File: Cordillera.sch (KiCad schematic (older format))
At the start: 29 parts, among them Q1 AO3400, Q2 AO3400, SW1 SW_SPST, U1 STM32F072CBTx, U2 XC6206P332MR, U3 SRV05-4

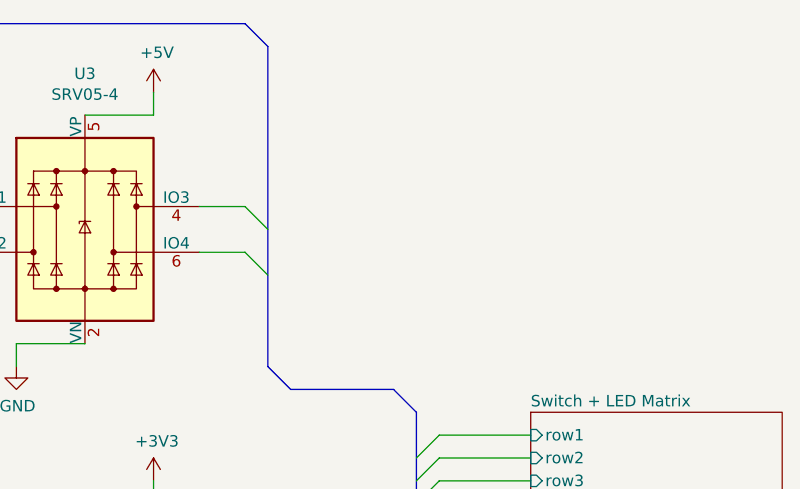
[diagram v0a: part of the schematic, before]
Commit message: Add indicator LEDs
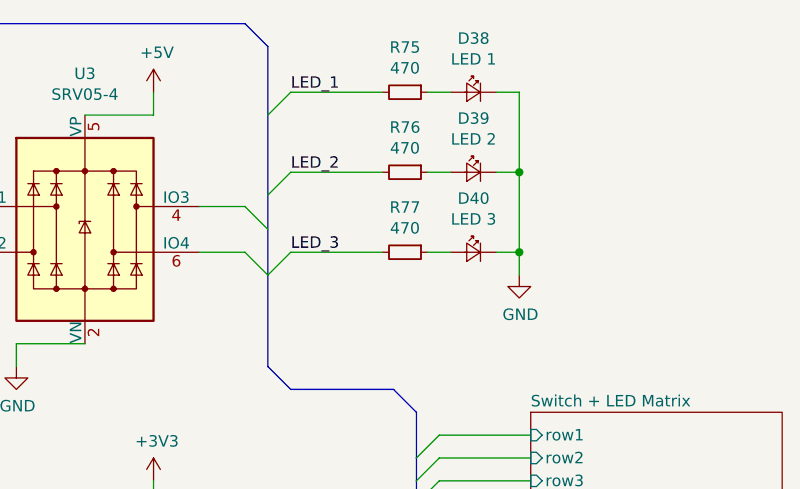
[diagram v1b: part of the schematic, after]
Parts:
- added D38: LED 1, keeb_lighting:LED_D3.0mm, symbol keeb_lighting:LED_Small
- added D39: LED 2, keeb_lighting:LED_D3.0mm, symbol keeb_lighting:LED_Small
- added D40: LED 3, keeb_lighting:LED_D3.0mm, symbol keeb_lighting:LED_Small
- added R75, R76, R77: 470, keeb_parts:R_0603_1608Metric, symbol keeb_parts:R_Small
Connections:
- net GND: now also D38.1 (K), D39.1 (K), D40.1 (K)
- new net: D38.2 (A), R75.1
- new net: D39.2 (A), R76.1
- new net: D40.2 (A), R77.1
- new net LED_1: R75.2
- new net LED_2: R76.2
- new net LED_3: R77.2
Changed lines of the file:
@@
+	1    0    0    -1
+$EndComp
+$Comp
+L keeb_lighting:LED_Small D38
+U 1 1 5F8AAE9D
+P 7450 1150
+F 0 "D38" H 7450 1385 50  0000 C CNN
+F 1 "LED 1" H 7450 1294 50  0000 C CNN
+F 2 "keeb_lighting:LED_D3.0mm" V 7450 1150 50  0001 C CNN
+F 3 "~" V 7450 1150 50  0001 C CNN
+	1    7450 1150
+	-1   0    0    -1
+$EndComp
+$Comp
+L keeb_lighting:LED_Small D39
+U 1 1 5F8AC84D
+P 7450 1500
+F 0 "D39" H 7450 1735 50  0000 C CNN
+F 1 "LED 2" H 7450 1644 50  0000 C CNN
+F 2 "keeb_lighting:LED_D3.0mm" V 7450 1500 50  0001 C CNN
+F 3 "~" V 7450 1500 50  0001 C CNN
+	1    7450 1500
+	-1   0    0    -1
+$EndComp
+$Comp
+L keeb_lighting:LED_Small D40
+U 1 1 5F8ACDD5
+P 7450 1850
+F 0 "D40" H 7450 2085 50  0000 C CNN
+F 1 "LED 3" H 7450 1994 50  0000 C CNN
+F 2 "keeb_lighting:LED_D3.0mm" V 7450 1850 50  0001 C CNN
+F 3 "~" V 7450 1850 50  0001 C CNN
+	1    7450 1850
+	-1   0    0    -1
+$EndComp
+$Comp
+L keeb_parts:R_Small R75
+U 1 1 5F8B84D2
+P 7150 1150
+F 0 "R75" V 6954 1150 50  0000 C CNN
+F 1 "470" V 7045 1150 50  0000 C CNN
+F 2 "keeb_parts:R_0603_1608Metric" H 7150 1150 50  0001 C CNN
+F 3 "~" H 7150 1150 50  0001 C CNN
+	1    7150 1150
+	0    1    1    0
+$EndComp
+Wire Wire Line
+	7350 1150 7250 1150
+$Comp
+L keeb_parts:R_Small R76
+U 1 1 5F8C72A6
+P 7150 1500
+F 0 "R76" V 6954 1500 50  0000 C CNN
+F 1 "470" V 7045 1500 50  0000 C CNN
+F 2 "keeb_parts:R_0603_1608Metric" H 7150 1500 50  0001 C CNN
+F 3 "~" H 7150 1500 50  0001 C CNN
+	1    7150 1500
+	0    1    1    0
+$EndComp
+Wire Wire Line
+	7350 1500 7250 1500
+$Comp
+L keeb_parts:R_Small R77
+U 1 1 5F8D1CE0
+P 7150 1850
+F 0 "R77" V 6954 1850 50  0000 C CNN
+F 1 "470" V 7045 1850 50  0000 C CNN
+F 2 "keeb_parts:R_0603_1608Metric" H 7150 1850 50  0001 C CNN
+F 3 "~" H 7150 1850 50  0001 C CNN
+	1    7150 1850
+	0    1    1    0
+$EndComp
+Wire Wire Line
+	7350 1850 7250 1850
+Wire Wire Line
+	7050 1500 6650 1500
+Entry Wire Line
+	6650 1500 6550 1600
+Text Label 6650 1500 0    50   ~ 0
+LED_2
+Wire Wire Line
+	7050 1850 6650 1850
+Entry Wire Line
+	6650 1850 6550 1950
+Text Label 6650 1850 0    50   ~ 0
+LED_3
+Wire Wire Line
+	7050 1150 6650 1150
+Entry Wire Line
+	6650 1150 6550 1250
+Text Label 6650 1150 0    50   ~ 0
+LED_1
+Wire Wire Line
+	7550 1150 7650 1150
+Wire Wire Line
+	7650 1150 7650 1500
+Wire Wire Line
+	7650 1850 7550 1850
+Wire Wire Line
+	7550 1500 7650 1500
+Connection ~ 7650 1500
+Wire Wire Line
+	7650 1500 7650 1850
+Wire Wire Line
+	7650 1850 7650 1950
+Connection ~ 7650 1850
+$Comp
+L keeb_power:GND #PWR0102
+U 1 1 5F93905E
+P 7650 1950
+F 0 "#PWR0102" H 7650 1700 50  0001 C CNN
+F 1 "GND" H 7655 1777 50  0000 C CNN
+F 2 "" H 7650 1950 50  0001 C CNN
+F 3 "" H 7650 1950 50  0001 C CNN
+	1    7650 1950
 	1    0    0    -1
 $EndComp

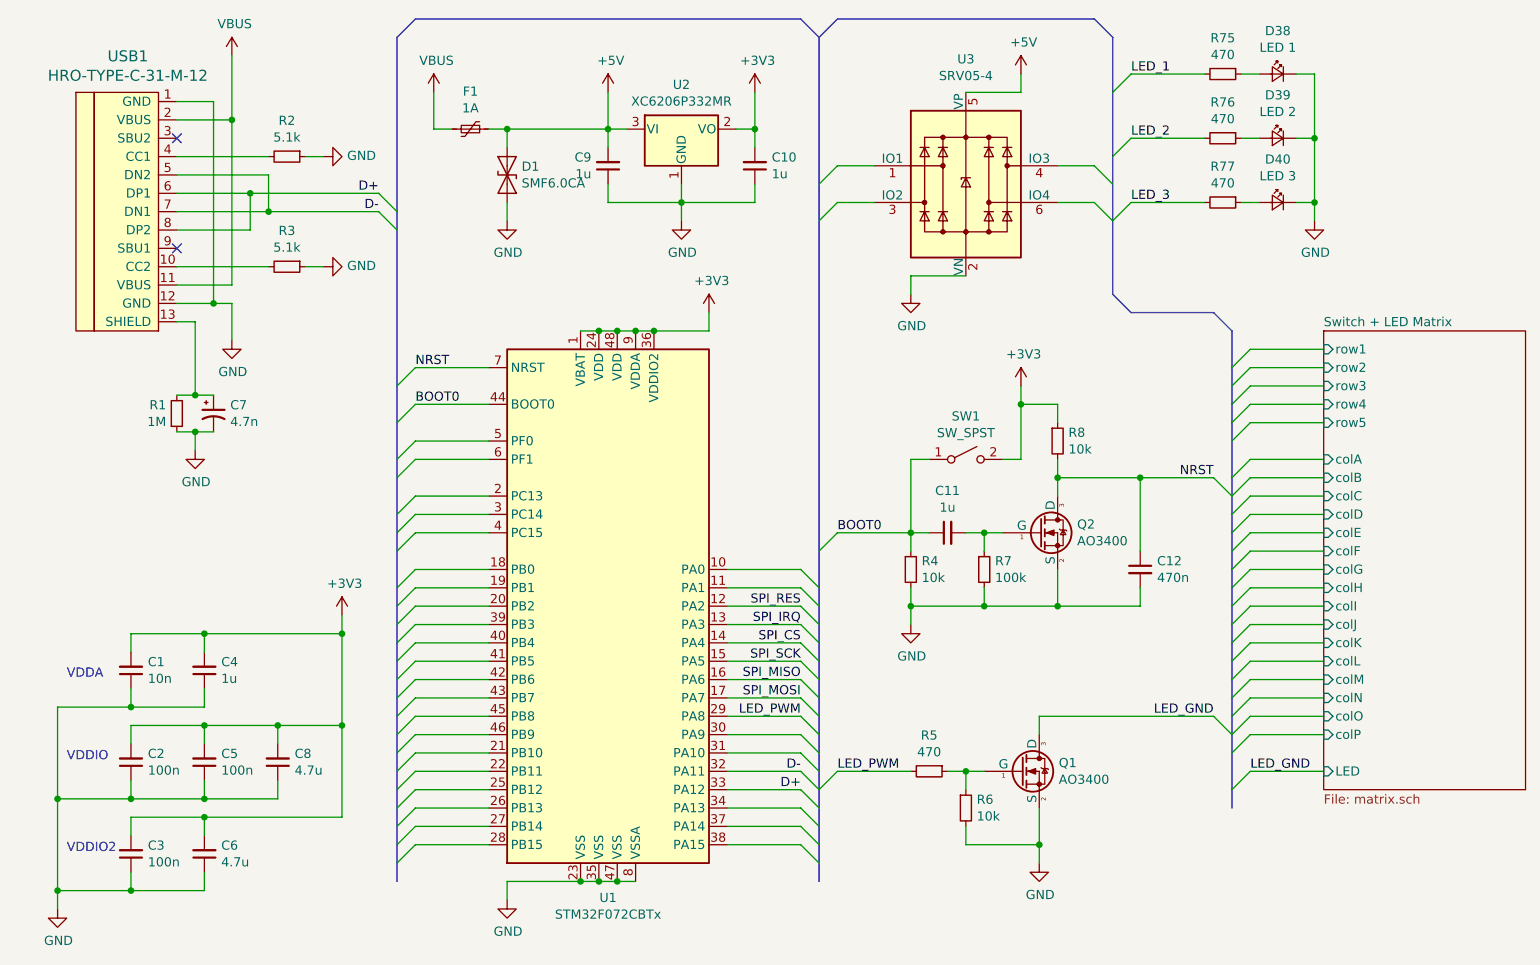
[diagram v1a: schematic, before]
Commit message: Finish routing switches
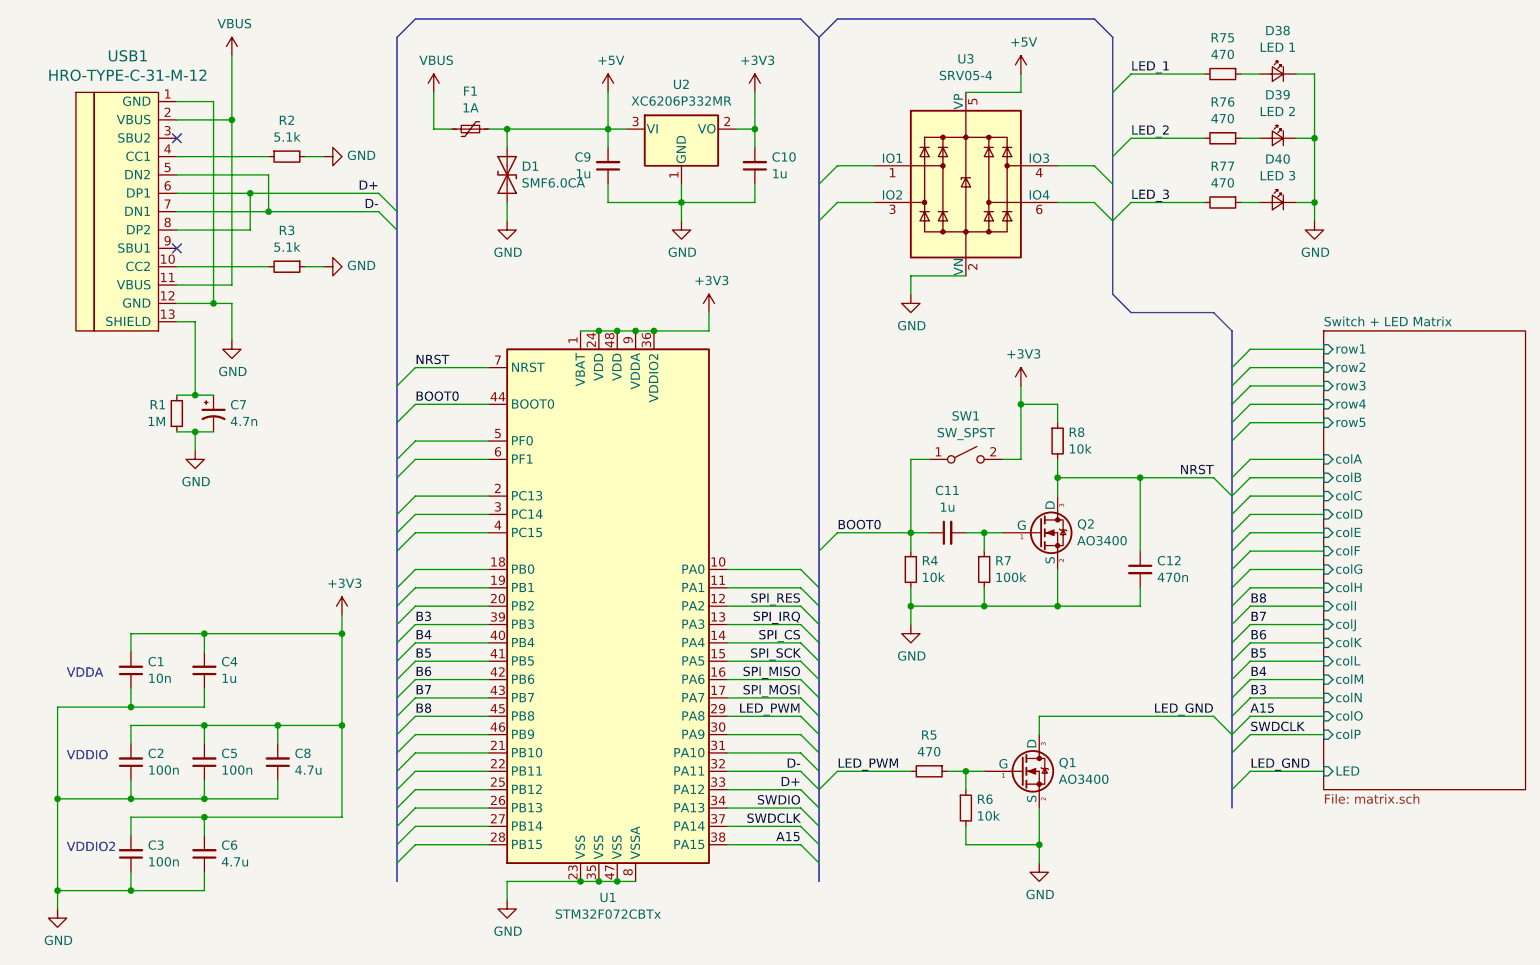
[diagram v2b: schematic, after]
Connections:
- net GND: now also R2.2; no longer R2.1
- net at USB1.4 (CC1): now also R2.1; no longer R2.2
- net SWDIO: now reaches U1.34 (PA13)
- net SWDCLK: now reaches U1.37 (PA14)
- net A15: now reaches U1.38 (PA15)
- net B3: now reaches U1.39 (PB3)
- net B4: now reaches U1.40 (PB4)
- net B5: now reaches U1.41 (PB5)
- net B6: now reaches U1.42 (PB6)
- net B7: now reaches U1.43 (PB7)
- net B8: now reaches U1.45 (PB8)
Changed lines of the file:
@@
 	1450 1600 1950 1600
-$Comp
-L keeb_parts:R_Small R2
-U 1 1 5F3187E0
-P 2050 1600
-F 0 "R2" V 1854 1600 50  0000 C CNN
-F 1 "5.1k" V 1945 1600 50  0000 C CNN
-F 2 "keeb_parts:R_0603_1608Metric" H 2050 1600 50  0001 C CNN
-F 3 "~" H 2050 1600 50  0001 C CNN
-	1    2050 1600
-	0    1    1    0
-$EndComp
 $Comp
 L keeb_parts:R_Small R3
@@
 	1    0    0    -1
 $EndComp
+Text Label 2750 4550 0    50   ~ 0
+B7
+Text Label 2750 4450 0    50   ~ 0
+B6
+Text Label 2750 4350 0    50   ~ 0
+B5
+Text Label 2750 4250 0    50   ~ 0
+B4
+Text Label 2750 4150 0    50   ~ 0
+B3
+Text Label 4850 5350 2    50   ~ 0
+A15
+Text Label 4850 5250 2    50   ~ 0
+SWDCLK
+Text Label 4850 5150 2    50   ~ 0
+SWDIO
+Text Label 2750 4650 0    50   ~ 0
+B8
+Text Label 7300 4750 0    50   ~ 0
+SWDCLK
+Text Label 7300 4650 0    50   ~ 0
+A15
+Text Label 7300 4550 0    50   ~ 0
+B3
+Text Label 7300 4450 0    50   ~ 0
+B4
+Text Label 7300 4350 0    50   ~ 0
+B5
+Text Label 7300 4250 0    50   ~ 0
+B6
+Text Label 7300 4150 0    50   ~ 0
+B7
+Text Label 7300 4050 0    50   ~ 0
+B8
+Wire Bus Line
+	7200 2550 7200 5150
 Wire Bus Line
 	6550 950  6550 2350
-Wire Bus Line
-	7200 2550 7200 5150
 Wire Bus Line
 	4950 950  4950 5550
 Wire Bus Line
 	2650 950  2650 5550
+$Comp
+L keeb_parts:R_Small R2
+U 1 1 5F3187E0
+P 2050 1600
+F 0 "R2" V 1854 1600 50  0000 C CNN
+F 1 "5.1k" V 1945 1600 50  0000 C CNN
+F 2 "keeb_parts:R_0603_1608Metric" H 2050 1600 50  0001 C CNN
+F 3 "~" H 2050 1600 50  0001 C CNN
+	1    2050 1600
+	0    -1   1    0
+$EndComp
 $EndSCHEMATC

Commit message: Finish column routing
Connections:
- net B2: now reaches U1.20 (PB2)
- net B10: now reaches U1.21 (PB10)
- net B11: now reaches U1.22 (PB11)
- net B12: now reaches U1.25 (PB12)
- net B13: now reaches U1.26 (PB13)
- net B14: now reaches U1.27 (PB14)
- net B15: now reaches U1.28 (PB15)
- net A9: now reaches U1.30 (PA9)
- net B9: now reaches U1.46 (PB9)
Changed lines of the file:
@@
 	7700 3050 7300 3050
-Wire Wire Line
-	7700 3250 7300 3250
-Wire Wire Line
-	7700 3350 7300 3350
-Wire Wire Line
-	7700 3450 7300 3450
-Wire Wire Line
-	7700 3550 7300 3550
-Wire Wire Line
-	7700 3650 7300 3650
-Wire Wire Line
-	7700 3750 7300 3750
 Wire Wire Line
 	7700 3850 7300 3850
@@
 Text Label 7300 4050 0    50   ~ 0
 B8
-Wire Bus Line
-	7200 2550 7200 5150
-Wire Bus Line
-	6550 950  6550 2350
-Wire Bus Line
-	4950 950  4950 5550
-Wire Bus Line
-	2650 950  2650 5550
 $Comp
 L keeb_parts:R_Small R2
@@
 	0    -1   1    0
 $EndComp
+Text Label 2750 4750 0    50   ~ 0
+B9
+Text Label 7300 2750 0    50   ~ 0
+B9
+Text Label 7300 2650 0    50   ~ 0
+SWDIO
+Text Label 4850 4750 2    50   ~ 0
+A9
+Text Label 7300 3950 0    50   ~ 0
+A9
+Text Label 2750 5050 0    50   ~ 0
+B12
+Text Label 2750 5150 0    50   ~ 0
+B13
+Text Label 2750 5250 0    50   ~ 0
+B14
+Text Label 2750 5350 0    50   ~ 0
+B15
+Wire Wire Line
+	7700 3550 7300 3550
+Wire Wire Line
+	7700 3450 7300 3450
+Wire Wire Line
+	7700 3350 7300 3350
+Wire Wire Line
+	7700 3250 7300 3250
+Text Label 7300 3550 0    50   ~ 0
+B12
+Text Label 7300 3450 0    50   ~ 0
+B13
+Text Label 7300 3350 0    50   ~ 0
+B14
+Text Label 7300 3250 0    50   ~ 0
+B15
+Text Label 2750 4950 0    50   ~ 0
+B11
+Text Label 2750 4850 0    50   ~ 0
+B10
+Wire Wire Line
+	7700 3750 7300 3750
+Wire Wire Line
+	7700 3650 7300 3650
+Text Label 7300 3650 0    50   ~ 0
+B11
+Text Label 7300 3750 0    50   ~ 0
+B10
+Wire Bus Line
+	6550 950  6550 2350
+Wire Bus Line
+	7200 2550 7200 5150
+Wire Bus Line
+	4950 950  4950 5550
+Wire Bus Line
+	2650 950  2650 5550
+Text Label 2750 4050 0    50   ~ 0
+B2
+Text Label 7300 3850 0    50   ~ 0
+B2
 $EndSCHEMATC

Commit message: Update files
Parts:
- added H1, H2: MountingHole, keeb_misc:mounting-circular, symbol keeb_parts:MountingHole
- added J1: Conn_01x08, keeb_connectors:PinHeader_2x04_P2.54mm_Vertical, symbol keeb_connectors:Conn_01x08
- C1, C10, C2, C3, C4, C5, C6, C7, C8, C9: footprint keeb_parts:R_0603_1608Metric -> keeb_parts:C_0603_1608Metric
- C11: value 1u -> 4.7u; footprint keeb_parts:R_0603_1608Metric -> keeb_parts:C_0603_1608Metric
- C12: value 470n -> 1u; footprint keeb_parts:R_0603_1608Metric -> keeb_parts:C_0603_1608Metric
- Q1, Q2: value AO3400 -> 2N7002
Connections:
- net LED_1 is gone; now on net B0: R75.2
- net LED_2 is gone; now on net A1: R76.2
- net LED_3 is gone; now on net A0: R77.2
- net +3V3: now also R8.2, J1.8 (Pin_8); no longer R8.1
- net D+: now also U3.1 (IO1), U3.3 (IO2)
- net D-: now also U3.4 (IO3), U3.6 (IO4)
- net GND: now also J1.7 (Pin_7)
- net NRST: now also R8.1; no longer R8.2
- net SPI_CS: now also J1.4 (Pin_4)
- net SPI_IRQ: now also J1.5 (Pin_5)
- net SPI_MISO: now also J1.2 (Pin_2)
- net SPI_MOSI: now also J1.3 (Pin_3)
- net SPI_RES: now also J1.6 (Pin_6)
- net SPI_SCK: now also J1.1 (Pin_1)
- net A0: now reaches U1.10 (PA0)
- net A1: now reaches U1.11 (PA1)
- net B0: now reaches U1.18 (PB0)
- net B1: now reaches U1.19 (PB1)
- net C13: now reaches U1.2 (PC13)
- net C14: now reaches U1.3 (PC14)
- net A10: now reaches U1.31 (PA10)
- net C15: now reaches U1.4 (PC15)
- net F0: now reaches U1.5 (PF0)
- net F1: now reaches U1.6 (PF1)
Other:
- moved on the sheet: C7, R1

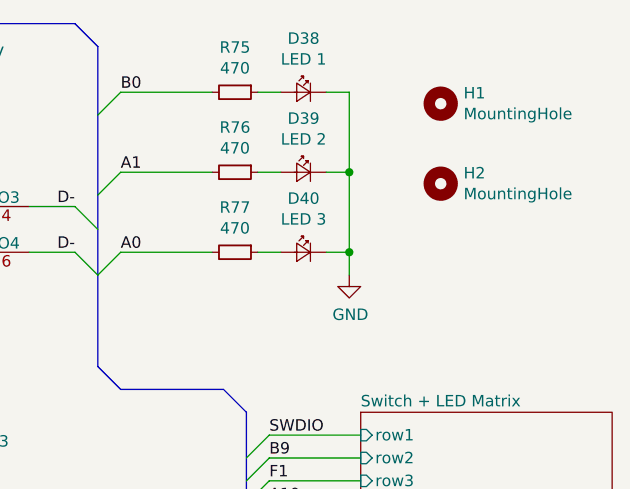
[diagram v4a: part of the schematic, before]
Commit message: fix indicator leds
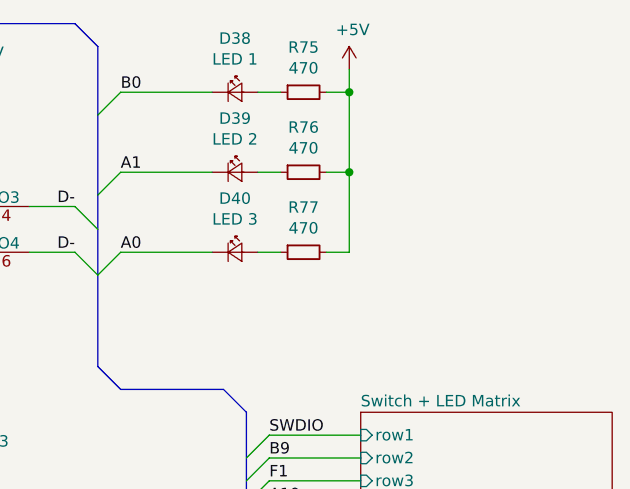
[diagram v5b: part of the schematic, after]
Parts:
- removed H1, H2: MountingHole, keeb_misc:mounting-circular, symbol keeb_parts:MountingHole
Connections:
- net +5V: now also R75.2, R76.2, R77.2
- net A0: now also D40.1 (K); no longer R77.2
- net A1: now also D39.1 (K); no longer R76.2
- net B0: now also D38.1 (K); no longer R75.2
- net GND: no longer D38.1 (K), D39.1 (K), D40.1 (K)
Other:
- moved on the sheet: D38, D39, D40, R75, R76, R77
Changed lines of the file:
@@
 L keeb_lighting:LED_Small D38
 U 1 1 5F8AAE9D
-P 7450 1150
-F 0 "D38" H 7450 1385 50  0000 C CNN
-F 1 "LED 1" H 7450 1294 50  0000 C CNN
-F 2 "keeb_lighting:LED_D3.0mm" V 7450 1150 50  0001 C CNN
-F 3 "~" V 7450 1150 50  0001 C CNN
-	1    7450 1150
-	-1   0    0    -1
+P 7150 1150
+F 0 "D38" H 7150 1385 50  0000 C CNN
+F 1 "LED 1" H 7150 1294 50  0000 C CNN
+F 2 "keeb_lighting:LED_D3.0mm" V 7150 1150 50  0001 C CNN
+F 3 "~" V 7150 1150 50  0001 C CNN
+	1    7150 1150
+	1    0    0    -1
 $EndComp
 $Comp
 L keeb_lighting:LED_Small D39
 U 1 1 5F8AC84D
-P 7450 1500
-F 0 "D39" H 7450 1735 50  0000 C CNN
-F 1 "LED 2" H 7450 1644 50  0000 C CNN
-F 2 "keeb_lighting:LED_D3.0mm" V 7450 1500 50  0001 C CNN
-F 3 "~" V 7450 1500 50  0001 C CNN
-	1    7450 1500
-	-1   0    0    -1
+P 7150 1500
+F 0 "D39" H 7150 1735 50  0000 C CNN
+F 1 "LED 2" H 7150 1644 50  0000 C CNN
+F 2 "keeb_lighting:LED_D3.0mm" V 7150 1500 50  0001 C CNN
+F 3 "~" V 7150 1500 50  0001 C CNN
+	1    7150 1500
+	1    0    0    -1
 $EndComp
 $Comp
 L keeb_lighting:LED_Small D40
 U 1 1 5F8ACDD5
-P 7450 1850
-F 0 "D40" H 7450 2085 50  0000 C CNN
-F 1 "LED 3" H 7450 1994 50  0000 C CNN
-F 2 "keeb_lighting:LED_D3.0mm" V 7450 1850 50  0001 C CNN
-F 3 "~" V 7450 1850 50  0001 C CNN
-	1    7450 1850
-	-1   0    0    -1
+P 7150 1850
+F 0 "D40" H 7150 2085 50  0000 C CNN
+F 1 "LED 3" H 7150 1994 50  0000 C CNN
+F 2 "keeb_lighting:LED_D3.0mm" V 7150 1850 50  0001 C CNN
+F 3 "~" V 7150 1850 50  0001 C CNN
+	1    7150 1850
+	1    0    0    -1
 $EndComp
 $Comp
 L keeb_parts:R_Small R75
 U 1 1 5F8B84D2
-P 7150 1150
-F 0 "R75" V 6954 1150 50  0000 C CNN
-F 1 "470" V 7045 1150 50  0000 C CNN
-F 2 "keeb_parts:R_0603_1608Metric" H 7150 1150 50  0001 C CNN
-F 3 "~" H 7150 1150 50  0001 C CNN
-	1    7150 1150
-	0    1    1    0
+P 7450 1150
+F 0 "R75" V 7254 1150 50  0000 C CNN
+F 1 "470" V 7345 1150 50  0000 C CNN
+F 2 "keeb_parts:R_0603_1608Metric" H 7450 1150 50  0001 C CNN
+F 3 "~" H 7450 1150 50  0001 C CNN
+	1    7450 1150
+	0    -1   1    0
 $EndComp
 Wire Wire Line
@@
 L keeb_parts:R_Small R76
 U 1 1 5F8C72A6
-P 7150 1500
-F 0 "R76" V 6954 1500 50  0000 C CNN
-F 1 "470" V 7045 1500 50  0000 C CNN
-F 2 "keeb_parts:R_0603_1608Metric" H 7150 1500 50  0001 C CNN
-F 3 "~" H 7150 1500 50  0001 C CNN
-	1    7150 1500
-	0    1    1    0
+P 7450 1500
+F 0 "R76" V 7254 1500 50  0000 C CNN
+F 1 "470" V 7345 1500 50  0000 C CNN
+F 2 "keeb_parts:R_0603_1608Metric" H 7450 1500 50  0001 C CNN
+F 3 "~" H 7450 1500 50  0001 C CNN
+	1    7450 1500
+	0    -1   1    0
 $EndComp
 Wire Wire Line
@@
 L keeb_parts:R_Small R77
 U 1 1 5F8D1CE0
-P 7150 1850
-F 0 "R77" V 6954 1850 50  0000 C CNN
-F 1 "470" V 7045 1850 50  0000 C CNN
-F 2 "keeb_parts:R_0603_1608Metric" H 7150 1850 50  0001 C CNN
-F 3 "~" H 7150 1850 50  0001 C CNN
-	1    7150 1850
-	0    1    1    0
+P 7450 1850
+F 0 "R77" V 7254 1850 50  0000 C CNN
+F 1 "470" V 7345 1850 50  0000 C CNN
+F 2 "keeb_parts:R_0603_1608Metric" H 7450 1850 50  0001 C CNN
+F 3 "~" H 7450 1850 50  0001 C CNN
+	1    7450 1850
+	0    -1   1    0
 $EndComp
 Wire Wire Line
@@
 Wire Wire Line
 	7650 1500 7650 1850
-Wire Wire Line
-	7650 1850 7650 1950
-Connection ~ 7650 1850
-$Comp
-L keeb_power:GND #PWR0102
-U 1 1 5F93905E
-P 7650 1950
-F 0 "#PWR0102" H 7650 1700 50  0001 C CNN
-F 1 "GND" H 7655 1777 50  0000 C CNN
-F 2 "" H 7650 1950 50  0001 C CNN
-F 3 "" H 7650 1950 50  0001 C CNN
-	1    7650 1950
-	1    0    0    -1
-$EndComp
 Text Label 2750 4550 0    50   ~ 0
 B7
@@
 	1850 3800 2550 3800
 $Comp
-L keeb_parts:MountingHole H1
-U 1 1 5F3A532E
-P 8050 1200
-F 0 "H1" H 8150 1246 50  0000 L CNN
-F 1 "MountingHole" H 8150 1155 50  0000 L CNN
-F 2 "keeb_misc:mounting-circular" H 8050 1200 50  0001 C CNN
-F 3 "~" H 8050 1200 50  0001 C CNN
-	1    8050 1200
-	1    0    0    -1
-$EndComp
-$Comp
-L keeb_parts:MountingHole H2
-U 1 1 5F3A5AB6
-P 8050 1550
-F 0 "H2" H 8150 1596 50  0000 L CNN
-F 1 "MountingHole" H 8150 1505 50  0000 L CNN
-F 2 "keeb_misc:mounting-circular" H 8050 1550 50  0001 C CNN
-F 3 "~" H 8050 1550 50  0001 C CNN
-	1    8050 1550
-	1    0    0    -1
-$EndComp
+L keeb_power:+5V #PWR0102
+U 1 1 5F48FA29
+P 7650 1050
+F 0 "#PWR0102" H 7650 900 50  0001 C CNN
+F 1 "+5V" H 7665 1223 50  0000 C CNN
+F 2 "" H 7650 1050 50  0001 C CNN
+F 3 "" H 7650 1050 50  0001 C CNN
+	1    7650 1050
+	1    0    0    -1
+$EndComp
+Wire Wire Line
+	7650 1050 7650 1150
+Connection ~ 7650 1150
 Wire Bus Line
 	6550 950  6550 2350
